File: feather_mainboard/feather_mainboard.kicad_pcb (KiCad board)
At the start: 2 copper layers, 60 x 60 mm, 44 parts, among them J1 62501021721, J2 62501021721, J3 61300211121, J4 693071020811, J5 61300211121, J6 61300211121, J7 61300211121, J8 61300211121, U1 Adafruit ESP32-S3 Feather, U2 SI2307CDS-T1-BE3, U3 2N7002K-T1-GE3, U4 WPME-FISM_SMT-8

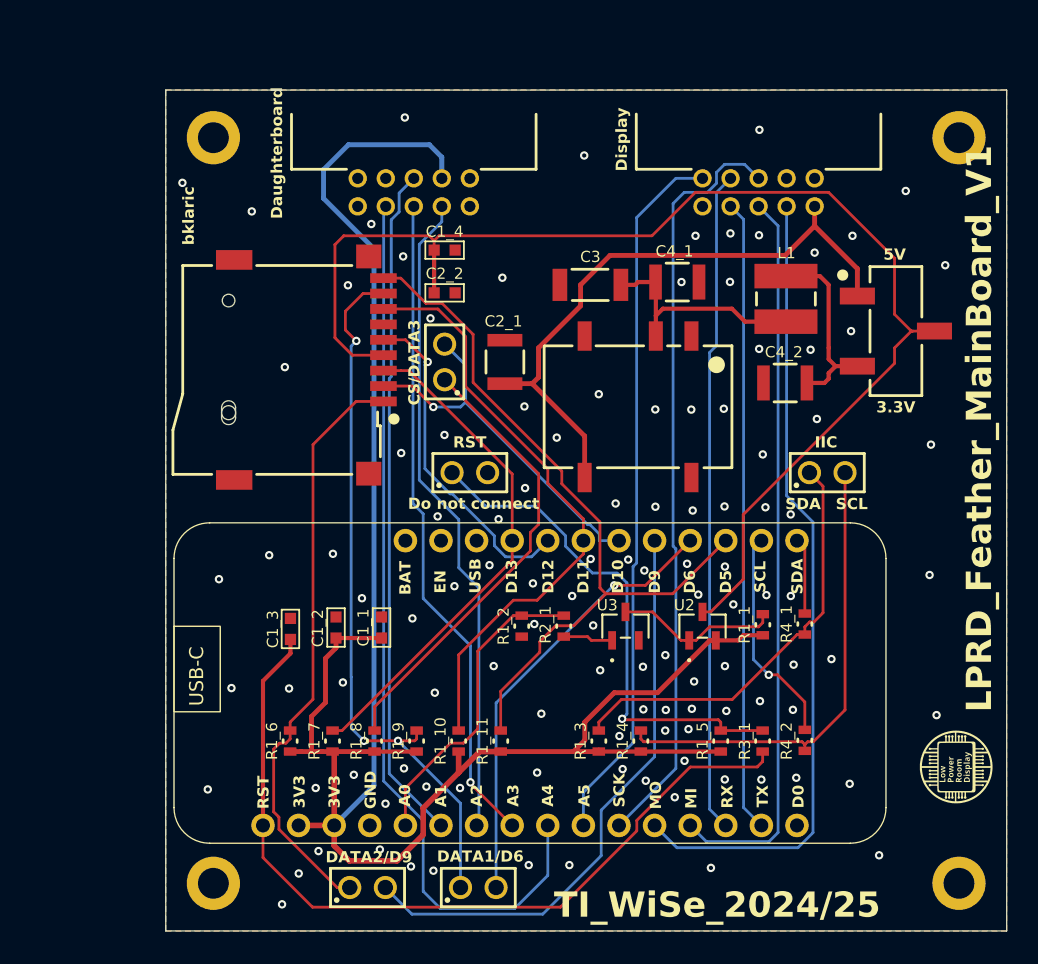
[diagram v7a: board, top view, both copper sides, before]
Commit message: added bigger logo and labeled the pins on the connectors
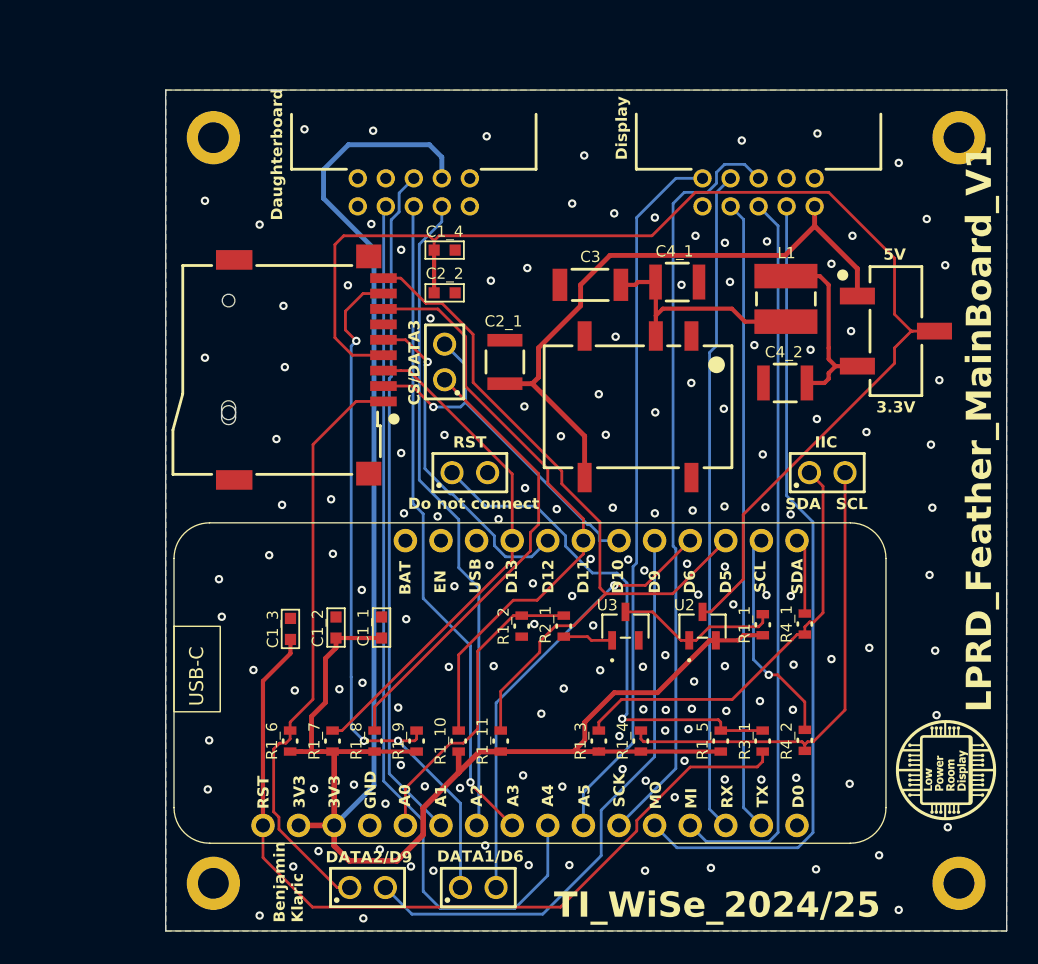
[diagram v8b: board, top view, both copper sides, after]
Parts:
- removed G**, G***: LOGO, Custom footprints:Logo
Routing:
- net GND: vias 113 -> 147
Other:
- board text added: "1"
- board text added: "10"
- board text added: "2"
- board text added: "9"
- board text added: "BSY"
- board text added: "B_1"
- board text added: "B_2"
- board text added: "B_3"
- board text added: "B_4"
- board text added: "Benjamin Klaric"
- board text added: "CS"
- board text added: "DC"
- board text added: "DIN"
- board text added: "GND"
- board text added: "SCK"
- board text added: "VCC"
- board text removed: "bklaric"
